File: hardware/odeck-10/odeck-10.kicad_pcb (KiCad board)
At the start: 6 copper layers, 110 x 75 mm, 4 parts

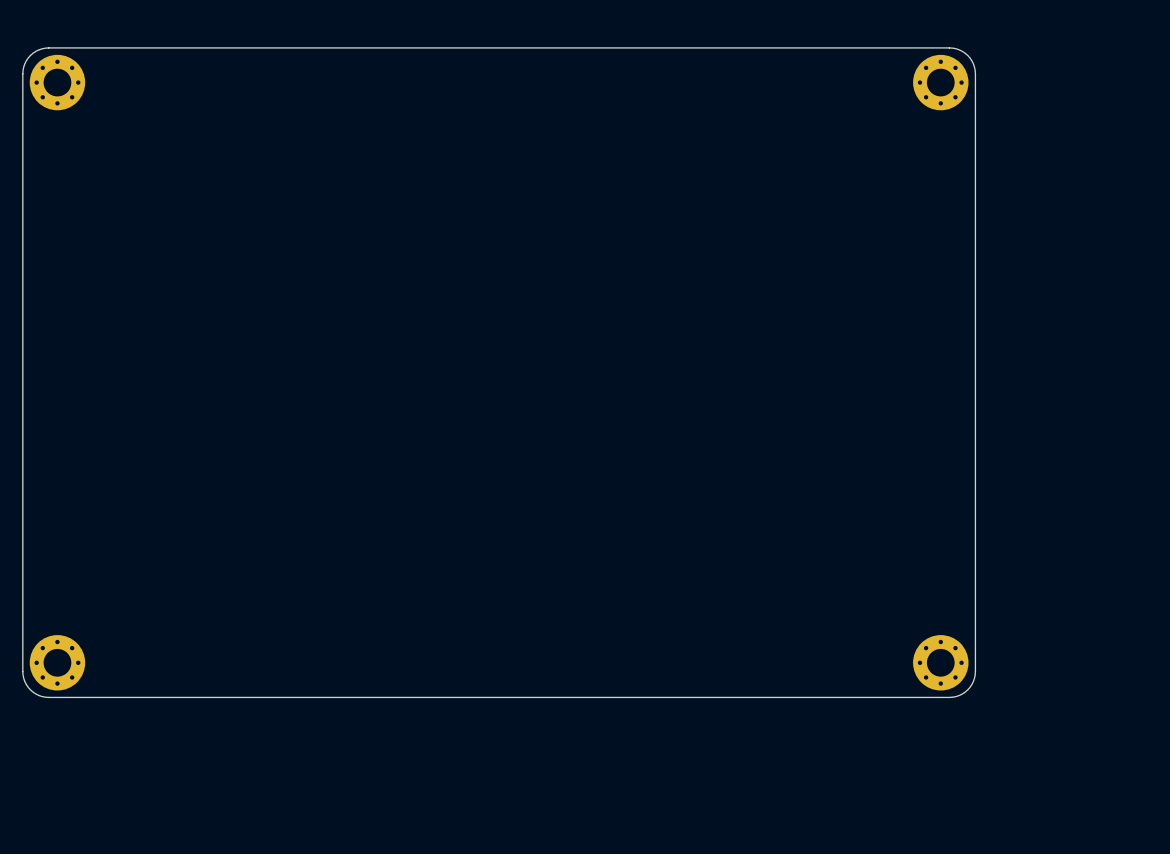
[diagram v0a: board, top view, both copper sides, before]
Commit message: Cost pass, PCB sync + rough placement, renders, README
- cost pass: extended parts 129 -> 114 (~$45/order less), nets unchanged
- tools/pcbsync.py: scripted update-PCB-from-schematic (keeps placed parts)
- tools/set_outline.py; board grown to 130x85 mm (provisional)
- hardware/odeck-10/placement.py: edge connectors + anchor-based packing,
  small passives spill to bottom; all 796 parts on the board (2 at anchor)
- docs/images: top/bottom/iso renders of the rough placement
- README.md: overview, architecture, repo layout, workflow, roadmap

Co-Authored-By: Claude Opus 5.5 <noreply@anthropic.com>
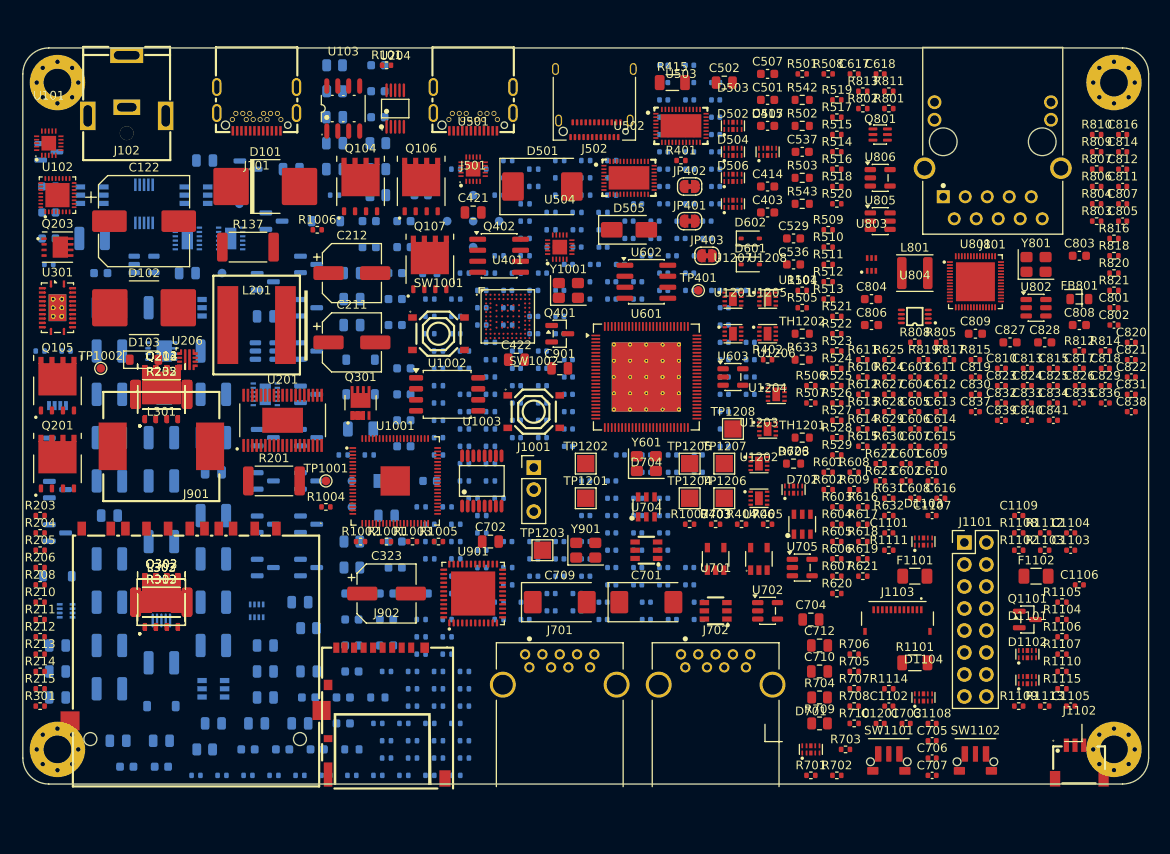
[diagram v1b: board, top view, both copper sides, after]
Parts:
- added C1001: 4.7u, Capacitor_SMD:C_0402_1005Metric, B.Cu at (156.0, 107.0)
- added C1002: 4.7u, Capacitor_SMD:C_0402_1005Metric, B.Cu at (157.0, 95.0)
- added C1003: 4.7u, Capacitor_SMD:C_0402_1005Metric, B.Cu at (157.0, 93.0)
- added C1004: 4.7u, Capacitor_SMD:C_0402_1005Metric, B.Cu at (157.0, 91.0)
- added C1005: 100n, Capacitor_SMD:C_0402_1005Metric, B.Cu at (157.0, 89.0)
- added C1006: 10u, Capacitor_SMD:C_0603_1608Metric, B.Cu at (144.0, 96.0)
- added C1007: 100n, Capacitor_SMD:C_0402_1005Metric, B.Cu at (157.0, 87.0)
- added C1008: 100n, Capacitor_SMD:C_0402_1005Metric, B.Cu at (157.0, 85.0)
- added C1009: 100n, Capacitor_SMD:C_0402_1005Metric, B.Cu at (158.0, 114.0)
- added C101: 2.2u/100V, Capacitor_SMD:C_1210_3225Metric, B.Cu at (108.0, 72.0)
- added C1010: 100n, Capacitor_SMD:C_0402_1005Metric, B.Cu at (158.0, 116.0)
- added C1011: 100n, Capacitor_SMD:C_0402_1005Metric, B.Cu at (159.0, 107.0)
- added C1012: 100n, Capacitor_SMD:C_0402_1005Metric, B.Cu at (159.0, 109.0)
- added C1013: 100n, Capacitor_SMD:C_0402_1005Metric, B.Cu at (159.0, 111.0)
- added C1014: 100n, Capacitor_SMD:C_0402_1005Metric, B.Cu at (159.0, 83.0)
- added C1015: 100n, Capacitor_SMD:C_0402_1005Metric, B.Cu at (160.0, 95.0)
- added C1016: 100n, Capacitor_SMD:C_0402_1005Metric, B.Cu at (160.0, 93.0)
- added C1017: 100n, Capacitor_SMD:C_0402_1005Metric, B.Cu at (160.0, 91.0)
- added C1018: 100n, Capacitor_SMD:C_0402_1005Metric, B.Cu at (160.0, 89.0)
- added C1019: 100n, Capacitor_SMD:C_0402_1005Metric, B.Cu at (160.0, 87.0)
- added C102: 100n/100V, Capacitor_SMD:C_0805_2012Metric, B.Cu at (121.0, 63.0)
- added C1020: 15p, Capacitor_SMD:C_0402_1005Metric, B.Cu at (160.0, 85.0)
- added C1021: 15p, Capacitor_SMD:C_0402_1005Metric, B.Cu at (161.0, 113.0)
- added C1022: 100n, Capacitor_SMD:C_0402_1005Metric, B.Cu at (161.0, 115.0)
- added C1023: 100n, Capacitor_SMD:C_0402_1005Metric, B.Cu at (159.0, 81.0)
- added C1024: 10n, Capacitor_SMD:C_0402_1005Metric, B.Cu at (162.0, 107.0)
- added C1025: 10n, Capacitor_SMD:C_0402_1005Metric, B.Cu at (162.0, 109.0)
- added C1026: 100n, Capacitor_SMD:C_0402_1005Metric, B.Cu at (162.0, 111.0)
- added C1027: 100n, Capacitor_SMD:C_0402_1005Metric, B.Cu at (162.0, 83.0)
- added C1028: 4.7u, Capacitor_SMD:C_0402_1005Metric, B.Cu at (162.0, 81.0)
- added C103: 100n/100V, Capacitor_SMD:C_0805_2012Metric, B.Cu at (119.0, 76.0)
- added C104: 1u, Capacitor_SMD:C_0402_1005Metric, B.Cu at (156.0, 78.0)
- added C105: 100n/50V, Capacitor_SMD:C_0603_1608Metric, B.Cu at (103.0, 66.0)
- added C106: 10u, Capacitor_SMD:C_0603_1608Metric, B.Cu at (103.0, 69.0)
- added C107: 10u, Capacitor_SMD:C_0603_1608Metric, B.Cu at (103.0, 72.0)
- added C108: 10u, Capacitor_SMD:C_0603_1608Metric, B.Cu at (109.0, 76.0)
- added C109: 220p, Capacitor_SMD:C_0603_1608Metric, B.Cu at (140.0, 70.0)
- added C110: 220p, Capacitor_SMD:C_0603_1608Metric, B.Cu at (140.0, 73.0)
- added C1101: 4.7u, Capacitor_SMD:C_0402_1005Metric, F.Cu at (200.0, 106.0)
- added C1102: 100n, Capacitor_SMD:C_0402_1005Metric, F.Cu at (200.0, 126.0)
- added C1103: 10n, Capacitor_SMD:C_0402_1005Metric, F.Cu at (221.0, 108.0)
- added C1104: 10n, Capacitor_SMD:C_0402_1005Metric, F.Cu at (221.0, 106.0)
- added C1105: 100n, Capacitor_SMD:C_0402_1005Metric, F.Cu at (221.0, 126.0)
- added C1106: 100n, Capacitor_SMD:C_0402_1005Metric, F.Cu at (222.0, 112.0)
- added C1107: 100n, Capacitor_SMD:C_0402_1005Metric, F.Cu at (205.0, 104.0)
- added C1108: 10n, Capacitor_SMD:C_0402_1005Metric, F.Cu at (205.0, 128.0)
- added C1109: 10n, Capacitor_SMD:C_0402_1005Metric, F.Cu at (215.0, 104.0)
- added C111: 100n, Capacitor_SMD:C_0402_1005Metric, B.Cu at (159.0, 78.0)
- added C112: 100n/100V, Capacitor_SMD:C_0805_2012Metric, B.Cu at (131.0, 64.0)
- added C113: 100n/50V, Capacitor_SMD:C_0603_1608Metric, B.Cu at (141.0, 58.0)
- added C114: 47n/100V, Capacitor_SMD:C_0603_1608Metric, B.Cu at (141.0, 55.0)
- added C115: 100n/100V, Capacitor_SMD:C_0805_2012Metric, B.Cu at (128.0, 81.0)
- added C116: 100n/100V, Capacitor_SMD:C_0805_2012Metric, B.Cu at (136.0, 64.0)
- added C117: 100n/50V, Capacitor_SMD:C_0603_1608Metric, B.Cu at (141.0, 52.0)
- added C118: 47n/100V, Capacitor_SMD:C_0603_1608Metric, B.Cu at (143.0, 76.0)
- added C119: 100n, Capacitor_SMD:C_0402_1005Metric, B.Cu at (160.0, 76.0)
- added C120: 100n, Capacitor_SMD:C_0402_1005Metric, B.Cu at (161.0, 73.0)
- added C1201: 100n, Capacitor_SMD:C_0402_1005Metric, F.Cu at (199.0, 128.0)
- added C1202: 100n, Capacitor_SMD:C_0402_1005Metric, B.Cu at (165.0, 102.0)
- added C1203: 100n, Capacitor_SMD:C_0402_1005Metric, B.Cu at (165.0, 100.0)
- added C1204: 100n, Capacitor_SMD:C_0402_1005Metric, B.Cu at (165.0, 104.0)
- added C1205: 100n, Capacitor_SMD:C_0402_1005Metric, B.Cu at (168.0, 102.0)
- added C1206: 100n, Capacitor_SMD:C_0402_1005Metric, B.Cu at (168.0, 100.0)
- added C1207: 100n, Capacitor_SMD:C_0402_1005Metric, B.Cu at (168.0, 104.0)
- added C1208: 100n, Capacitor_SMD:C_0402_1005Metric, B.Cu at (165.0, 98.0)
- added C121: 100n, Capacitor_SMD:C_0402_1005Metric, B.Cu at (162.0, 78.0)
- added C122: 47u/100V, Capacitor_SMD:CP_Elec_10x10, F.Cu at (114.0, 70.0)
- added C123: 1u/100V, Capacitor_SMD:C_0805_2012Metric, B.Cu at (136.0, 61.0)
- added C124: 100n/100V, Capacitor_SMD:C_0805_2012Metric, B.Cu at (136.0, 58.0)
- added C125: 100n, Capacitor_SMD:C_0402_1005Metric, B.Cu at (163.0, 75.0)
- added C201: 4.7u/100V, Capacitor_SMD:C_1210_3225Metric, B.Cu at (116.0, 95.0)
- added C202: 4.7u/100V, Capacitor_SMD:C_1210_3225Metric, B.Cu at (110.0, 90.0)
- added C203: 4.7u/100V, Capacitor_SMD:C_1210_3225Metric, B.Cu at (122.0, 90.0)
- added C204: 4.7u/100V, Capacitor_SMD:C_1210_3225Metric, B.Cu at (110.0, 85.0)
- added C205: 10u/50V, Capacitor_SMD:C_1210_3225Metric, B.Cu at (122.0, 85.0)
- added C206: 10u/50V, Capacitor_SMD:C_1210_3225Metric, B.Cu at (110.0, 95.0)
- added C207: 10u/50V, Capacitor_SMD:C_1210_3225Metric, B.Cu at (122.0, 95.0)
- added C208: 10u/50V, Capacitor_SMD:C_1210_3225Metric, B.Cu at (116.0, 80.0)
- added C209: 10u/50V, Capacitor_SMD:C_1210_3225Metric, B.Cu at (116.0, 100.0)
- added C210: 10u/50V, Capacitor_SMD:C_1210_3225Metric, B.Cu at (110.0, 80.0)
- added C211: 100u/35V, Capacitor_SMD:CP_Elec_6.3x7.7, F.Cu at (138.0, 84.0)
- added C212: 100u/35V, Capacitor_SMD:CP_Elec_6.3x7.7, F.Cu at (138.0, 76.0)
- added C213: 100n/50V, Capacitor_SMD:C_0603_1608Metric, B.Cu at (138.0, 113.0)
- added C214: 100n/100V, Capacitor_SMD:C_0805_2012Metric, B.Cu at (122.0, 99.0)
- added C215: 1u/100V, Capacitor_SMD:C_0805_2012Metric, B.Cu at (110.0, 104.0)
- added C216: 1u/50V, Capacitor_SMD:C_0603_1608Metric, B.Cu at (138.0, 116.0)
- added C217: 22u, Capacitor_SMD:C_0805_2012Metric, B.Cu at (138.0, 82.0)
- added C218: 22u, Capacitor_SMD:C_0805_2012Metric, B.Cu at (138.0, 79.0)
- added C219: 100n/50V, Capacitor_SMD:C_0603_1608Metric, B.Cu at (142.0, 113.0)
- added C220: 100n/50V, Capacitor_SMD:C_0603_1608Metric, B.Cu at (142.0, 116.0)
- added C221: 100p, Capacitor_SMD:C_0402_1005Metric, B.Cu at (163.0, 90.0)
- added C222: 22n, Capacitor_SMD:C_0402_1005Metric, B.Cu at (163.0, 88.0)
- added C223: 6.8n, Capacitor_SMD:C_0603_1608Metric, B.Cu at (143.0, 82.0)
- added C224: 82p, Capacitor_SMD:C_0402_1005Metric, B.Cu at (163.0, 92.0)
- added C225: 1n, Capacitor_SMD:C_0402_1005Metric, B.Cu at (163.0, 86.0)
- added C226: 4.7u, Capacitor_SMD:C_0603_1608Metric, B.Cu at (143.0, 79.0)
- added C227: 4.7n, Capacitor_SMD:C_0402_1005Metric, B.Cu at (163.0, 94.0)
- added C228: 100n/50V, Capacitor_SMD:C_0603_1608Metric, B.Cu at (143.0, 107.0)
- added C229: 100n/50V, Capacitor_SMD:C_0603_1608Metric, B.Cu at (143.0, 110.0)
- added C230: 22n/50V, Capacitor_SMD:C_0603_1608Metric, B.Cu at (144.0, 90.0)
- added C231: 100n, Capacitor_SMD:C_0402_1005Metric, B.Cu at (163.0, 96.0)
- added C232: 100n, Capacitor_SMD:C_0402_1005Metric, B.Cu at (164.0, 73.0)
- added C233: 10u/50V, Capacitor_SMD:C_1210_3225Metric, B.Cu at (110.0, 100.0)
- added C234: 100n/50V, Capacitor_SMD:C_0603_1608Metric, B.Cu at (144.0, 87.0)
- added C235: 100n/50V, Capacitor_SMD:C_0603_1608Metric, B.Cu at (144.0, 93.0)
- added C236: 100n/50V, Capacitor_SMD:C_0603_1608Metric, B.Cu at (144.0, 73.0)
- added C237: 100n/50V, Capacitor_SMD:C_0603_1608Metric, B.Cu at (144.0, 70.0)
- added C238: 1u/50V, Capacitor_SMD:C_0603_1608Metric, B.Cu at (138.0, 119.0)
- added C239: 3.3n, Capacitor_SMD:C_0603_1608Metric, B.Cu at (142.0, 119.0)
- added C240: 1n, Capacitor_SMD:C_0402_1005Metric, B.Cu at (164.0, 71.0)
- added C241: 10u, Capacitor_SMD:C_0805_2012Metric, B.Cu at (138.0, 76.0)
- added C242: 100n, Capacitor_SMD:C_0402_1005Metric, B.Cu at (164.0, 113.0)
- added C243: 2.2n, Capacitor_SMD:C_0603_1608Metric, B.Cu at (146.0, 67.0)
- added C244: 100n, Capacitor_SMD:C_0402_1005Metric, B.Cu at (164.0, 115.0)
- added C301: 4.7u/100V, Capacitor_SMD:C_1210_3225Metric, B.Cu at (110.0, 114.0)
- added C302: 4.7u/100V, Capacitor_SMD:C_1210_3225Metric, B.Cu at (122.0, 114.0)
- added C303: 4.7u/100V, Capacitor_SMD:C_1210_3225Metric, B.Cu at (110.0, 109.0)
- added C304: 4.7u/100V, Capacitor_SMD:C_1210_3225Metric, B.Cu at (122.0, 109.0)
- added C305: 100n/100V, Capacitor_SMD:C_0805_2012Metric, B.Cu at (104.0, 119.0)
- added C306: 100n/100V, Capacitor_SMD:C_0805_2012Metric, B.Cu at (128.0, 119.0)
- added C307: 100n, Capacitor_SMD:C_0402_1005Metric, B.Cu at (165.0, 111.0)
- added C308: 1n/100V, Capacitor_SMD:C_0603_1608Metric, B.Cu at (126.0, 131.0)
- added C309: 47u/10V, Capacitor_SMD:C_1210_3225Metric, B.Cu at (110.0, 119.0)
- added C310: 47u/10V, Capacitor_SMD:C_1210_3225Metric, B.Cu at (122.0, 119.0)
- added C311: 47u/10V, Capacitor_SMD:C_1210_3225Metric, B.Cu at (116.0, 107.0)
- added C312: 47u/10V, Capacitor_SMD:C_1210_3225Metric, B.Cu at (116.0, 121.0)
- added C313: 47u/10V, Capacitor_SMD:C_1210_3225Metric, B.Cu at (110.0, 124.0)
- added C314: 47u/10V, Capacitor_SMD:C_1210_3225Metric, B.Cu at (122.0, 104.0)
- added C315: 1u/100V, Capacitor_SMD:C_0805_2012Metric, B.Cu at (104.0, 122.0)
- added C316: 4.7u, Capacitor_SMD:C_0603_1608Metric, B.Cu at (133.0, 125.0)
- added C317: 100n, Capacitor_SMD:C_0402_1005Metric, B.Cu at (165.0, 109.0)
- added C318: 10n, Capacitor_SMD:C_0402_1005Metric, B.Cu at (165.0, 107.0)
- added C319: 100p, Capacitor_SMD:C_0402_1005Metric, B.Cu at (165.0, 79.0)
- added C320: 100n/50V, Capacitor_SMD:C_0603_1608Metric, B.Cu at (130.0, 131.0)
- added C321: 100n/50V, Capacitor_SMD:C_0603_1608Metric, B.Cu at (134.0, 131.0)
- added C322: 100n, Capacitor_SMD:C_0402_1005Metric, B.Cu at (165.0, 77.0)
- added C323: 330u/6.3V, Capacitor_SMD:CP_Elec_6.3x5.9, F.Cu at (142.0, 113.0)
- added C324: 22u, Capacitor_SMD:C_0805_2012Metric, B.Cu at (128.0, 122.0)
- added C325: 22u, Capacitor_SMD:C_0805_2012Metric, B.Cu at (104.0, 125.0)
- added C326: 10u, Capacitor_SMD:C_0805_2012Metric, B.Cu at (128.0, 125.0)
- added C327: 10u, Capacitor_SMD:C_0805_2012Metric, B.Cu at (122.0, 128.0)
- added C328: 100n, Capacitor_SMD:C_0402_1005Metric, B.Cu at (166.0, 75.0)
- added C329: 22n, Capacitor_SMD:C_0402_1005Metric, B.Cu at (167.0, 114.0)
- added C330: 100n, Capacitor_SMD:C_0402_1005Metric, B.Cu at (167.0, 116.0)
- added C331: 22u, Capacitor_SMD:C_0805_2012Metric, B.Cu at (127.0, 128.0)
- added C332: 22u, Capacitor_SMD:C_0805_2012Metric, B.Cu at (116.0, 130.0)
- added C333: 22u, Capacitor_SMD:C_0805_2012Metric, B.Cu at (132.0, 114.0)
- added C334: 10u, Capacitor_SMD:C_0805_2012Metric, B.Cu at (111.0, 130.0)
- added C335: 10u, Capacitor_SMD:C_0805_2012Metric, B.Cu at (132.0, 128.0)
- added C336: 100n, Capacitor_SMD:C_0402_1005Metric, B.Cu at (167.0, 73.0)
- added C337: 100n, Capacitor_SMD:C_0402_1005Metric, B.Cu at (167.0, 71.0)
- added C338: 22u, Capacitor_SMD:C_0603_1608Metric, B.Cu at (116.0, 133.0)
- added C339: 22u, Capacitor_SMD:C_0603_1608Metric, B.Cu at (112.0, 133.0)
- added C340: 22u, Capacitor_SMD:C_0603_1608Metric, B.Cu at (137.0, 125.0)
- added C341: 22u, Capacitor_SMD:C_0603_1608Metric, B.Cu at (137.0, 128.0)
- added C401: 1u, Capacitor_SMD:C_0402_1005Metric, B.Cu at (168.0, 77.0)
- added C402: 100n, Capacitor_SMD:C_0402_1005Metric, B.Cu at (168.0, 79.0)
- added C403: 4.7u, Capacitor_SMD:C_0603_1608Metric, F.Cu at (186.0, 69.0)
- added C404: 100n, Capacitor_SMD:C_0402_1005Metric, B.Cu at (169.0, 75.0)
- added C405: 1u, Capacitor_SMD:C_0402_1005Metric, B.Cu at (170.0, 70.0)
- added C406: 100n, Capacitor_SMD:C_0402_1005Metric, B.Cu at (170.0, 72.0)
- added C407: 100n, Capacitor_SMD:C_0402_1005Metric, B.Cu at (171.0, 68.0)
- added C408: 1u, Capacitor_SMD:C_0402_1005Metric, B.Cu at (171.0, 66.0)
- added C409: 100n, Capacitor_SMD:C_0402_1005Metric, B.Cu at (171.0, 64.0)
- added C410: 100n, Capacitor_SMD:C_0402_1005Metric, B.Cu at (171.0, 77.0)
- added C411: 100n, Capacitor_SMD:C_0402_1005Metric, B.Cu at (171.0, 79.0)
- added C412: 1u, Capacitor_SMD:C_0402_1005Metric, B.Cu at (172.0, 74.0)
- added C413: 1u, Capacitor_SMD:C_0402_1005Metric, B.Cu at (173.0, 70.0)
- added C414: 100n/50V, Capacitor_SMD:C_0603_1608Metric, F.Cu at (186.0, 66.0)
- added C415: 100n/50V, Capacitor_SMD:C_0603_1608Metric, F.Cu at (186.0, 59.0)
- added C416: 390p, Capacitor_SMD:C_0402_1005Metric, B.Cu at (173.0, 72.0)
- added C417: 390p, Capacitor_SMD:C_0402_1005Metric, B.Cu at (174.0, 68.0)
- added C418: 390p, Capacitor_SMD:C_0402_1005Metric, B.Cu at (174.0, 66.0)
- added C419: 390p, Capacitor_SMD:C_0402_1005Metric, B.Cu at (174.0, 64.0)
- added C420: 100n, Capacitor_SMD:C_0402_1005Metric, B.Cu at (174.0, 76.0)
- added C421: 10u, Capacitor_SMD:C_0805_2012Metric, F.Cu at (152.0, 69.0)
- added C422: 10u, Capacitor_SMD:C_0805_2012Metric, F.Cu at (157.0, 86.0)
- added C501: 100n/50V, Capacitor_SMD:C_0603_1608Metric, F.Cu at (186.0, 56.0)
- added C502: 100n/100V, Capacitor_SMD:C_0805_2012Metric, F.Cu at (181.0, 54.0)
- added C503: 1u, Capacitor_SMD:C_0402_1005Metric, B.Cu at (174.0, 62.0)
- added C504: 100n, Capacitor_SMD:C_0402_1005Metric, B.Cu at (174.0, 60.0)
- added C505: 100n, Capacitor_SMD:C_0402_1005Metric, B.Cu at (174.0, 58.0)
- added C506: 100n, Capacitor_SMD:C_0402_1005Metric, B.Cu at (174.0, 56.0)
- added C507: 10u, Capacitor_SMD:C_0603_1608Metric, F.Cu at (186.0, 53.0)
- added C508: 100n, Capacitor_SMD:C_0402_1005Metric, B.Cu at (174.0, 54.0)
- added C509: 220n, Capacitor_SMD:C_0402_1005Metric, B.Cu at (174.0, 52.0)
- added C510: 220n, Capacitor_SMD:C_0402_1005Metric, B.Cu at (175.0, 74.0)
- added C511: 220n, Capacitor_SMD:C_0402_1005Metric, B.Cu at (176.0, 70.0)
- added C512: 220n, Capacitor_SMD:C_0402_1005Metric, B.Cu at (176.0, 72.0)
- added C513: 220n, Capacitor_SMD:C_0402_1005Metric, B.Cu at (174.0, 78.0)
- added C514: 220n, Capacitor_SMD:C_0402_1005Metric, B.Cu at (177.0, 62.0)
- added C515: 220n, Capacitor_SMD:C_0402_1005Metric, B.Cu at (177.0, 60.0)
- added C516: 220n, Capacitor_SMD:C_0402_1005Metric, B.Cu at (177.0, 64.0)
- added C517: 220n, Capacitor_SMD:C_0402_1005Metric, B.Cu at (177.0, 58.0)
- added C518: 220n, Capacitor_SMD:C_0402_1005Metric, B.Cu at (177.0, 66.0)
- added C519: 220n, Capacitor_SMD:C_0402_1005Metric, B.Cu at (177.0, 56.0)
- added C520: 220n, Capacitor_SMD:C_0402_1005Metric, B.Cu at (177.0, 68.0)
- added C521: 220n, Capacitor_SMD:C_0402_1005Metric, B.Cu at (177.0, 54.0)
- added C522: 220n, Capacitor_SMD:C_0402_1005Metric, B.Cu at (177.0, 52.0)
- added C523: 100n, Capacitor_SMD:C_0402_1005Metric, B.Cu at (177.0, 76.0)
- added C524: 100n, Capacitor_SMD:C_0402_1005Metric, B.Cu at (177.0, 78.0)
- added C525: 100n, Capacitor_SMD:C_0402_1005Metric, B.Cu at (178.0, 74.0)
- added C526: 100n, Capacitor_SMD:C_0402_1005Metric, B.Cu at (179.0, 70.0)
- added C527: 100n, Capacitor_SMD:C_0402_1005Metric, B.Cu at (179.0, 72.0)
- added C528: 100n, Capacitor_SMD:C_0402_1005Metric, B.Cu at (180.0, 62.0)
- added C529: 10u, Capacitor_SMD:C_0603_1608Metric, F.Cu at (189.0, 72.0)
- added C530: 220n, Capacitor_SMD:C_0402_1005Metric, B.Cu at (180.0, 60.0)
- added C531: 220n, Capacitor_SMD:C_0402_1005Metric, B.Cu at (180.0, 64.0)
- added C532: 220n, Capacitor_SMD:C_0402_1005Metric, B.Cu at (180.0, 58.0)
- added C533: 220n, Capacitor_SMD:C_0402_1005Metric, B.Cu at (180.0, 66.0)
- added C534: 220n, Capacitor_SMD:C_0402_1005Metric, B.Cu at (180.0, 56.0)
- added C535: 220n, Capacitor_SMD:C_0402_1005Metric, B.Cu at (180.0, 68.0)
- added C536: 100n/50V, Capacitor_SMD:C_0603_1608Metric, F.Cu at (189.0, 75.0)
- added C537: 100n/50V, Capacitor_SMD:C_0603_1608Metric, F.Cu at (190.0, 62.0)
- added C538: 1u, Capacitor_SMD:C_0402_1005Metric, B.Cu at (180.0, 54.0)
- added C601: 220n, Capacitor_SMD:C_0402_1005Metric, F.Cu at (202.0, 98.0)
- added C602: 220n, Capacitor_SMD:C_0402_1005Metric, F.Cu at (202.0, 100.0)
- added C603: 220n, Capacitor_SMD:C_0402_1005Metric, F.Cu at (203.0, 88.0)
- added C604: 220n, Capacitor_SMD:C_0402_1005Metric, F.Cu at (203.0, 90.0)
- added C605: 220n, Capacitor_SMD:C_0402_1005Metric, F.Cu at (203.0, 92.0)
- added C606: 220n, Capacitor_SMD:C_0402_1005Metric, F.Cu at (203.0, 94.0)
- added C607: 220n, Capacitor_SMD:C_0402_1005Metric, F.Cu at (203.0, 96.0)
- added C608: 220n, Capacitor_SMD:C_0402_1005Metric, F.Cu at (203.0, 102.0)
- added C609: 220n, Capacitor_SMD:C_0402_1005Metric, F.Cu at (205.0, 98.0)
- added C610: 220n, Capacitor_SMD:C_0402_1005Metric, F.Cu at (205.0, 100.0)
- added C611: 220n, Capacitor_SMD:C_0402_1005Metric, F.Cu at (206.0, 88.0)
- added C612: 220n, Capacitor_SMD:C_0402_1005Metric, F.Cu at (206.0, 90.0)
- added C613: 100n, Capacitor_SMD:C_0402_1005Metric, F.Cu at (206.0, 92.0)
- added C614: 100n, Capacitor_SMD:C_0402_1005Metric, F.Cu at (206.0, 94.0)
- added C615: 100n, Capacitor_SMD:C_0402_1005Metric, F.Cu at (206.0, 96.0)
- added C616: 100n, Capacitor_SMD:C_0402_1005Metric, F.Cu at (206.0, 102.0)
- added C617: 100n, Capacitor_SMD:C_0402_1005Metric, F.Cu at (196.0, 53.0)
- added C618: 100n, Capacitor_SMD:C_0402_1005Metric, F.Cu at (199.0, 53.0)
- added C619: 100n, Capacitor_SMD:C_0402_1005Metric, B.Cu at (172.0, 97.0)
- added C620: 100n, Capacitor_SMD:C_0402_1005Metric, B.Cu at (181.0, 88.0)
- added C621: 4.7u, Capacitor_SMD:C_0402_1005Metric, B.Cu at (181.0, 86.0)
- added C622: 4.7u, Capacitor_SMD:C_0402_1005Metric, B.Cu at (181.0, 90.0)
- added C623: 1n, Capacitor_SMD:C_0402_1005Metric, B.Cu at (169.0, 97.0)
- added C624: 100n, Capacitor_SMD:C_0402_1005Metric, B.Cu at (175.0, 97.0)
- added C625: 100n, Capacitor_SMD:C_0402_1005Metric, B.Cu at (181.0, 84.0)
- added C626: 100n, Capacitor_SMD:C_0402_1005Metric, B.Cu at (181.0, 92.0)
- added C627: 100n, Capacitor_SMD:C_0402_1005Metric, B.Cu at (181.0, 82.0)
- added C628: 100n, Capacitor_SMD:C_0402_1005Metric, B.Cu at (178.0, 97.0)
- added C629: 100n, Capacitor_SMD:C_0402_1005Metric, B.Cu at (181.0, 94.0)
- added C630: 100n, Capacitor_SMD:C_0402_1005Metric, B.Cu at (181.0, 80.0)
- added C631: 100n, Capacitor_SMD:C_0402_1005Metric, B.Cu at (181.0, 96.0)
- added C632: 100n, Capacitor_SMD:C_0402_1005Metric, B.Cu at (180.0, 78.0)
- added C633: 4.7u, Capacitor_SMD:C_0402_1005Metric, B.Cu at (181.0, 98.0)
- added C634: 4.7u, Capacitor_SMD:C_0402_1005Metric, B.Cu at (172.0, 99.0)
- added C635: 4.7u, Capacitor_SMD:C_0402_1005Metric, B.Cu at (175.0, 99.0)
- added C636: 1n, Capacitor_SMD:C_0402_1005Metric, B.Cu at (178.0, 99.0)
- added C637: 20p, Capacitor_SMD:C_0402_1005Metric, B.Cu at (183.0, 78.0)
- added C638: 20p, Capacitor_SMD:C_0402_1005Metric, B.Cu at (184.0, 88.0)
- added C639: 1n, Capacitor_SMD:C_0402_1005Metric, B.Cu at (184.0, 86.0)
- added C640: 100n, Capacitor_SMD:C_0402_1005Metric, B.Cu at (184.0, 90.0)
- added C641: 100n, Capacitor_SMD:C_0402_1005Metric, B.Cu at (184.0, 84.0)
- added C701: 150u/10V, Capacitor_Tantalum_SMD:CP_EIA-7343-31_Kemet-D, F.Cu at (172.0, 114.0)
- added C702: 10u, Capacitor_SMD:C_0805_2012Metric, F.Cu at (154.0, 107.0)
- added C703: 100n, Capacitor_SMD:C_0402_1005Metric, F.Cu at (202.0, 128.0)
- added C704: 10u, Capacitor_SMD:C_0805_2012Metric, F.Cu at (191.0, 116.0)
- added C705: 100n, Capacitor_SMD:C_0402_1005Metric, F.Cu at (205.0, 130.0)
- added C706: 100n, Capacitor_SMD:C_0402_1005Metric, F.Cu at (205.0, 132.0)
- added C707: 100n, Capacitor_SMD:C_0402_1005Metric, F.Cu at (205.0, 134.0)
- added C708: 100n, Capacitor_SMD:C_0402_1005Metric, B.Cu at (172.0, 116.0)
- added C709: 150u/10V, Capacitor_Tantalum_SMD:CP_EIA-7343-31_Kemet-D, F.Cu at (162.0, 114.0)
- added C710: 10u, Capacitor_SMD:C_0805_2012Metric, F.Cu at (192.0, 122.0)
- added C711: 100n, Capacitor_SMD:C_0402_1005Metric, B.Cu at (175.0, 116.0)
- added C712: 10u, Capacitor_SMD:C_0805_2012Metric, F.Cu at (192.0, 119.0)
- added C713: 100n, Capacitor_SMD:C_0402_1005Metric, B.Cu at (178.0, 116.0)
- added C714: 100n, Capacitor_SMD:C_0402_1005Metric, B.Cu at (172.0, 114.0)
- added C715: 100n, Capacitor_SMD:C_0402_1005Metric, B.Cu at (175.0, 114.0)
- added C716: 100n, Capacitor_SMD:C_0402_1005Metric, B.Cu at (178.0, 114.0)
- added C801: 1u, Capacitor_SMD:C_0402_1005Metric, F.Cu at (226.0, 80.0)
- added C802: 1n, Capacitor_SMD:C_0402_1005Metric, F.Cu at (226.0, 82.0)
- added C803: 10u, Capacitor_SMD:C_0603_1608Metric, F.Cu at (222.0, 74.0)
- added C804: 22u, Capacitor_SMD:C_0603_1608Metric, F.Cu at (198.0, 79.0)
- added C805: 100n, Capacitor_SMD:C_0402_1005Metric, F.Cu at (227.0, 70.0)
- added C806: 10u, Capacitor_SMD:C_0603_1608Metric, F.Cu at (198.0, 82.0)
- added C807: 100n, Capacitor_SMD:C_0402_1005Metric, F.Cu at (227.0, 68.0)
- added C808: 22u, Capacitor_SMD:C_0603_1608Metric, F.Cu at (222.0, 82.0)
- added C809: 22u, Capacitor_SMD:C_0603_1608Metric, F.Cu at (210.0, 83.0)
- added C810: 100n, Capacitor_SMD:C_0402_1005Metric, F.Cu at (213.0, 87.0)
- added C811: 2.2u, Capacitor_SMD:C_0402_1005Metric, F.Cu at (227.0, 66.0)
- added C812: 100n, Capacitor_SMD:C_0402_1005Metric, F.Cu at (227.0, 64.0)
- added C813: 100n, Capacitor_SMD:C_0402_1005Metric, F.Cu at (216.0, 87.0)
- added C814: 100n, Capacitor_SMD:C_0402_1005Metric, F.Cu at (227.0, 62.0)
- added C815: 2.2u, Capacitor_SMD:C_0402_1005Metric, F.Cu at (219.0, 87.0)
- added C816: 2.2u, Capacitor_SMD:C_0402_1005Metric, F.Cu at (227.0, 60.0)
- added C817: 100n, Capacitor_SMD:C_0402_1005Metric, F.Cu at (222.0, 87.0)
- added C818: 100n, Capacitor_SMD:C_0402_1005Metric, F.Cu at (225.0, 87.0)
- added C819: 100n, Capacitor_SMD:C_0402_1005Metric, F.Cu at (210.0, 88.0)
- added C820: 2.2u, Capacitor_SMD:C_0402_1005Metric, F.Cu at (228.0, 84.0)
- added C821: 2.2u, Capacitor_SMD:C_0402_1005Metric, F.Cu at (228.0, 86.0)
- added C822: 2.2u, Capacitor_SMD:C_0402_1005Metric, F.Cu at (228.0, 88.0)
- added C823: 100n, Capacitor_SMD:C_0402_1005Metric, F.Cu at (213.0, 89.0)
- added C824: 100n, Capacitor_SMD:C_0402_1005Metric, F.Cu at (216.0, 89.0)
- added C825: 100n, Capacitor_SMD:C_0402_1005Metric, F.Cu at (219.0, 89.0)
- added C826: 2.2u, Capacitor_SMD:C_0402_1005Metric, F.Cu at (222.0, 89.0)
- added C827: 10u, Capacitor_SMD:C_0603_1608Metric, F.Cu at (214.0, 84.0)
- added C828: 10u, Capacitor_SMD:C_0603_1608Metric, F.Cu at (218.0, 84.0)
- added C829: 100n, Capacitor_SMD:C_0402_1005Metric, F.Cu at (225.0, 89.0)
- added C830: 2.2u, Capacitor_SMD:C_0402_1005Metric, F.Cu at (210.0, 90.0)
- added C831: 100n, Capacitor_SMD:C_0402_1005Metric, F.Cu at (228.0, 90.0)
- added C832: 1u, Capacitor_SMD:C_0402_1005Metric, F.Cu at (213.0, 91.0)
- added C833: 20p, Capacitor_SMD:C_0402_1005Metric, F.Cu at (216.0, 91.0)
- added C834: 20p, Capacitor_SMD:C_0402_1005Metric, F.Cu at (219.0, 91.0)
- added C835: 100n, Capacitor_SMD:C_0402_1005Metric, F.Cu at (222.0, 91.0)
- added C836: 100n, Capacitor_SMD:C_0402_1005Metric, F.Cu at (225.0, 91.0)
- added C837: 390p, Capacitor_SMD:C_0402_1005Metric, F.Cu at (210.0, 92.0)
- added C838: 100n, Capacitor_SMD:C_0402_1005Metric, F.Cu at (228.0, 92.0)
- added C839: 100n, Capacitor_SMD:C_0402_1005Metric, F.Cu at (213.0, 93.0)
- added C840: 100n, Capacitor_SMD:C_0402_1005Metric, F.Cu at (216.0, 93.0)
- added C841: 100n, Capacitor_SMD:C_0402_1005Metric, F.Cu at (219.0, 93.0)
- added C901: 10u, Capacitor_SMD:C_0805_2012Metric, F.Cu at (162.0, 87.0)
- added C902: 100n, Capacitor_SMD:C_0402_1005Metric, B.Cu at (168.0, 112.0)
- added C903: 10u, Capacitor_SMD:C_0603_1608Metric, B.Cu at (138.0, 122.0)
- added C904: 1u, Capacitor_SMD:C_0402_1005Metric, B.Cu at (168.0, 110.0)
- added C905: 100n, Capacitor_SMD:C_0402_1005Metric, B.Cu at (168.0, 108.0)
- added C906: 100n, Capacitor_SMD:C_0402_1005Metric, B.Cu at (168.0, 106.0)
- added C907: 100n, Capacitor_SMD:C_0402_1005Metric, B.Cu at (171.0, 112.0)
- added C908: 100n, Capacitor_SMD:C_0402_1005Metric, B.Cu at (171.0, 110.0)
- added C909: 2.2u, Capacitor_SMD:C_0402_1005Metric, B.Cu at (171.0, 108.0)
- added C910: 1u, Capacitor_SMD:C_0402_1005Metric, B.Cu at (171.0, 106.0)
- added C911: 1u, Capacitor_SMD:C_0402_1005Metric, B.Cu at (171.0, 104.0)
- added C912: 1u, Capacitor_SMD:C_0402_1005Metric, B.Cu at (171.0, 102.0)
- added C913: 4.7u, Capacitor_SMD:C_0402_1005Metric, B.Cu at (174.0, 112.0)
- added C914: 100n, Capacitor_SMD:C_0402_1005Metric, B.Cu at (174.0, 110.0)
- added C915: 4.7u, Capacitor_SMD:C_0402_1005Metric, B.Cu at (174.0, 108.0)
- added C916: 100n, Capacitor_SMD:C_0402_1005Metric, B.Cu at (174.0, 106.0)
- added C917: 100n, Capacitor_SMD:C_0402_1005Metric, B.Cu at (174.0, 104.0)
- added C918: 100n, Capacitor_SMD:C_0402_1005Metric, B.Cu at (174.0, 102.0)
- added C919: 20p, Capacitor_SMD:C_0402_1005Metric, B.Cu at (177.0, 112.0)
- added C920: 20p, Capacitor_SMD:C_0402_1005Metric, B.Cu at (177.0, 110.0)
- added D1001: PWR green, LED_SMD:LED_0805_2012Metric, B.Cu at (142.0, 104.0)
- added D1002: STATUS red, LED_SMD:LED_0603_1608Metric, B.Cu at (147.0, 100.0)
- added D101: 5.0SMDJ51A, odeck:SMC_L6.9-W5.9-LS7.9-RD, F.Cu at (128.0, 66.0)
- added D102: 5.0SMDJ48CA, odeck:SMC_L6.9-W5.9-LS7.9-BI, F.Cu at (114.0, 80.0)
- added D103: 1N4148W, Diode_SMD:D_SOD-123, F.Cu at (114.0, 86.0)
- added D1101: TPD4E02B04, odeck:USON-10_L2.5-W1.0-P0.50-BL, F.Cu at (216.0, 120.0)
- added D1102: TPD4E02B04, odeck:USON-10_L2.5-W1.0-P0.50-BL, F.Cu at (216.0, 123.0)
- added D1103: TPD4E02B04, odeck:USON-10_L2.5-W1.0-P0.50-BL, F.Cu at (204.0, 107.0)
- added D1104: TPD4E02B04, odeck:USON-10_L2.5-W1.0-P0.50-BL, F.Cu at (204.0, 125.0)
- added D201: 1N4148W, Diode_SMD:D_SOD-123, B.Cu at (135.0, 70.0)
- added D202: BZT52C5V1, Diode_SMD:D_SOD-123, B.Cu at (104.0, 111.0)
- added D203: BAT54A, Package_TO_SOT_SMD:SOT-23, B.Cu at (128.0, 95.0)
- added D204: BAT46W, Diode_SMD:D_SOD-123, B.Cu at (139.0, 90.0)
- added D205: BAV70, Package_TO_SOT_SMD:SOT-23, B.Cu at (104.0, 96.0)
- added D206: 1N4148W, Diode_SMD:D_SOD-123, B.Cu at (139.0, 86.0)
- added D301: BAT46W, Diode_SMD:D_SOD-123, B.Cu at (116.0, 126.0)
- added D501: SMCJ28A, Diode_SMD:D_SMC, F.Cu at (160.0, 66.0)
- added D502: TPD4E02B04, odeck:USON-10_L2.5-W1.0-P0.50-BL, F.Cu at (182.0, 62.0)
- added D503: TPD4E02B04, odeck:USON-10_L2.5-W1.0-P0.50-BL, F.Cu at (182.0, 59.0)
- added D504: TPD4E02B04, odeck:USON-10_L2.5-W1.0-P0.50-BL, F.Cu at (182.0, 65.0)
- added D505: SMAJ6.0A, Diode_SMD:D_SMA, F.Cu at (170.0, 71.0)
- added D506: TPD4E02B04, odeck:USON-10_L2.5-W1.0-P0.50-BL, F.Cu at (182.0, 68.0)
- added D507: TPD4E02B04, odeck:USON-10_L2.5-W1.0-P0.50-BL, F.Cu at (186.0, 62.0)
- added D601: BAT54WS, Diode_SMD:D_SOD-323, F.Cu at (184.0, 75.0)
- added D602: BAT54WS, Diode_SMD:D_SOD-323, F.Cu at (184.0, 72.0)
- added D701: TPD4E02B04, odeck:USON-10_L2.5-W1.0-P0.50-BL, F.Cu at (191.0, 131.0)
- added D702: USBLC6-2SC6, odeck:SOT-23-6_L2.9-W1.6-P0.95-LS2.8-BL, F.Cu at (190.0, 105.0)
- added D703: TPD4E02B04, odeck:USON-10_L2.5-W1.0-P0.50-BL, F.Cu at (189.0, 101.0)
- added D704: USBLC6-2SC6, odeck:SOT-23-6_L2.9-W1.6-P0.95-LS2.8-BL, F.Cu at (172.0, 103.0)
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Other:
- board size 110 x 75 mm -> 130 x 85 mm

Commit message: Placement: floorplan, per-region placement scripts, DRC-clean placed board
- docs/floorplan.md: 5 regions; board 130x89 mm (SD socket depth), microSD on
  top at the front-right (overhangs edge 2 mm under the LCD panel)
- layout/{power,usbc,hubrails,front,right}.py + zz_integration.py; per-block
  placement rationale and routing intent in docs/layout-notes/
- tools/apply_layout.py (region/ownership/overlap checks), set_outline.py,
  pcbsync --refresh, apply_routing.py (coupled pairs, via pairs, zones),
  autoroute.py (Freerouting 2.4, headless, analytics off)
- schematic: R908 22R microSD CLK series termination
- footprints: PMG1 closed courtyard, barrel peg NPTH
- DRC rules (.kicad_dru): edge parts, HS pair spacing, HV clearance;
  HS netclass pad clearance 0.15
- DRC: 0 violations (499 unrouted, as expected); renders updated

Co-Authored-By: Claude Opus 5.5 <noreply@anthropic.com>
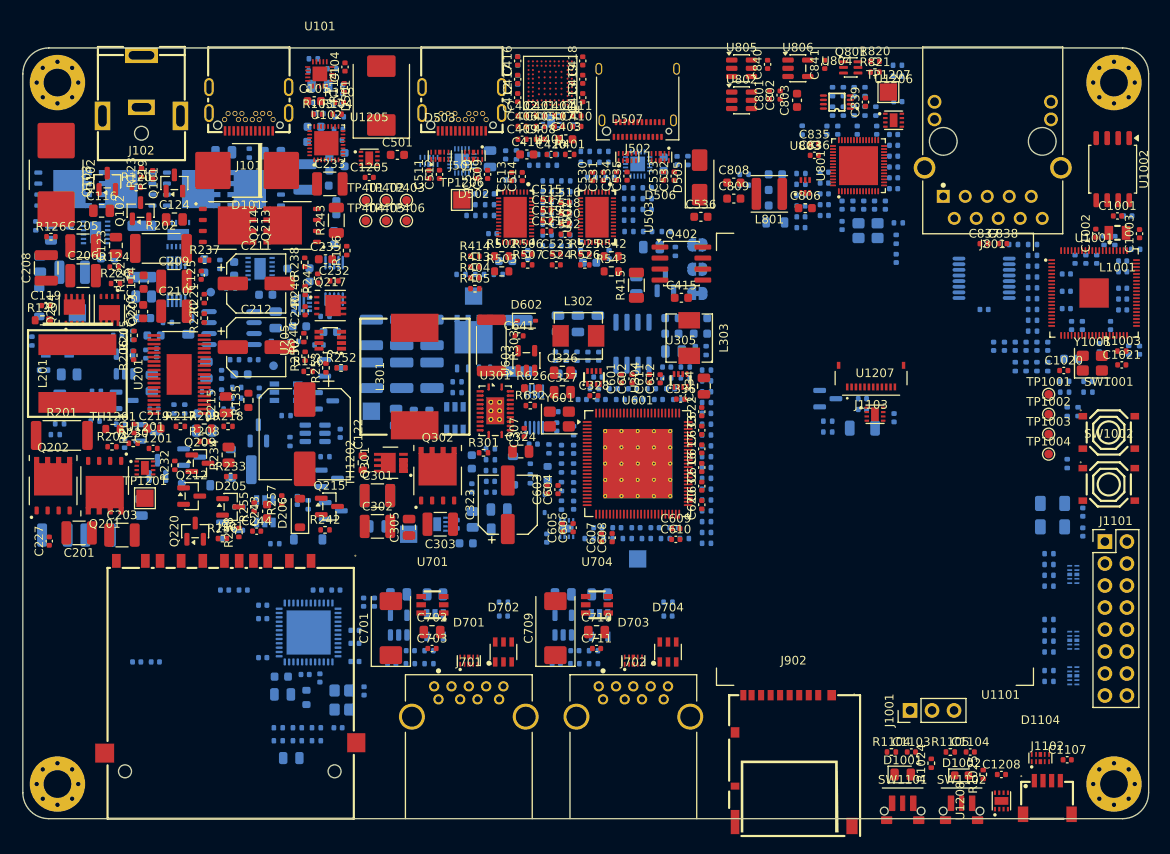
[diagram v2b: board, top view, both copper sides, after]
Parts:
- added R908: 22, Resistor_SMD:R_0402_1005Metric, B.Cu at (129.1, 107.2)
- C1001, C1002, C1003, C1020, C1021, C104, C105, C114, C116, C119, C1205, C1208, C123, C124, C125, C201, C203, C205, C206, C208, C209, C210, C215, C219, C220, C227, C232, C233, C235, C240, C243, C244, C301, C302, C303, C305, C307, C324, C326, C327, C328, C334, C336, C401, C402, C404, C405, C406, C407, C408, C409, C410, C411, C412, C413, C416, C417, C418, C419, C420, C509, C510, C511, C512, C513, C514, C515, C516, C517, C518, C519, C520, C521, C522, C523, C524, C530, C531, C532, C533, C534, C535, C620, C622, C632, C633, C641, C711, D1001, D1002, D205, D206, L1001, Q101, Q102, Q103, Q204, Q209, Q212, Q215, Q217, Q220, R1024, R1025, R103, R104, R110, R114, R116, R119, R120, R122, R123, R124, R126, R130, R135, R136, R209, R217, R218, R220, R221, R226, R230, R232, R233, R234, R237, R238, R242, R243, R244, R246, R247, R250, R252, R253, R255, R256, R257, R258, R413, R414, TP1003, TP1004, TP402, TP403, TP404, TP405, TP406, U205, U304, U305: moved to F.Cu
- C1101, C1102, C1105, C1106, C1108, C1109, C421, C422, C502, C507, C529, C537, C613, C614, C615, C618, C704, C705, C706, C707, C712, C804, C805, C807, C810, C811, C812, C813, C814, C815, C816, C817, C818, C819, C820, C821, C822, C823, C824, C825, C826, C827, C828, C829, C830, C831, C832, C833, C834, C901, D103, D1101, D1102, D1103, D504, D601, F1101, F1102, FB801, JP401, JP402, JP403, Q104, Q105, Q106, Q107, Q1101, Q303, Q401, R1001, R1002, R1004, R1005, R1006, R1007, R101, R1101, R1102, R1103, R1106, R1107, R1108, R1109, R1110, R1111, R1112, R1113, R1114, R1115, R137, R210, R211, R212, R213, R214, R215, R235, R312, R402, R403, R501, R504, R505, R508, R509, R510, R511, R512, R513, R514, R515, R516, R517, R518, R519, R520, R521, R522, R523, R524, R527, R528, R529, R601, R602, R603, R604, R605, R606, R607, R608, R609, R610, R611, R612, R613, R614, R615, R616, R617, R618, R619, R620, R621, R622, R623, R624, R625, R627, R628, R629, R630, R631, R633, R701, R702, R703, R704, R705, R706, R707, R708, R709, R710, R801, R802, R803, R804, R805, R806, R807, R808, R809, R810, R811, R812, R813, R814, R815, R816, R817, R818, R819, TP1202, TP1203, TP1204, TP1205, TP1208, U1003, U103, U1202, U1203, U1204, U204, U206, U501, U504, U602, U702, U703, U705, U706, U901, Y801, Y901: moved to B.Cu
- moved TP1002 109.6 mm to (218.4, 92.3)
- moved R1001 92.9 mm to (228.5, 73.2)
- moved R1002 91.4 mm to (227.7, 84.9), turned to 90 degrees
- moved R1006 90.7 mm to (220.6, 98.0), turned to 90 degrees
- moved C1201 89.8 mm to (115.0, 96.2)
- moved R1008 89.6 mm to (226.1, 72.2), turned to 90 degrees
- moved L1001 89.1 mm to (226.4, 71.3), turned to 180 degrees
- moved R1004 87.5 mm to (221.8, 92.0), turned to 90 degrees
- moved R1003 84.8 mm to (226.9, 85.0)
- moved C339 84.1 mm to (178.2, 81.2)
- moved TP1001 84.0 mm to (218.4, 90.0)
- moved U1001 83.6 mm to (223.7, 78.3)
- moved R1010 82.9 mm to (216.6, 74.0)
- moved U1002 81.1 mm to (225.8, 64.0), turned to -90 degrees
- moved C1022 80.7 mm to (227.6, 69.4)
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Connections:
- J902 pad 5: /Card reader/CR_USD_CLK -> /Card reader/CR_USD_CLK_S
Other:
- board size 130 x 85 mm -> 130 x 89 mm

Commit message: Placement fixes for routing; DRC rules scoped so net classes don't break fine-pitch pads
- hubrails: C611/C612 swap, C603-C608 rotated (pad 1 to hub pin), C609/C610
  east, pin 99 via room, VBUS-detect parts repacked
- right: C835/C836 rotated, RP2350 USB via room
- usbc: U501 south, U504/U503 straps rearranged for downstream escape vias
- zz_integration: R908 at the U901 CLK escape, TP1206/TP1202 moved
- power: C220/C114/R122 to bottom (sense pair + VIN via room)
- net class clearances 0.15; HV 0.3 mm spacing only for drawn copper
- DRC: 0 errors (unrouted only); docs/routing-notes/placement-fixes.md

Co-Authored-By: Claude Opus 5.5 <noreply@anthropic.com>
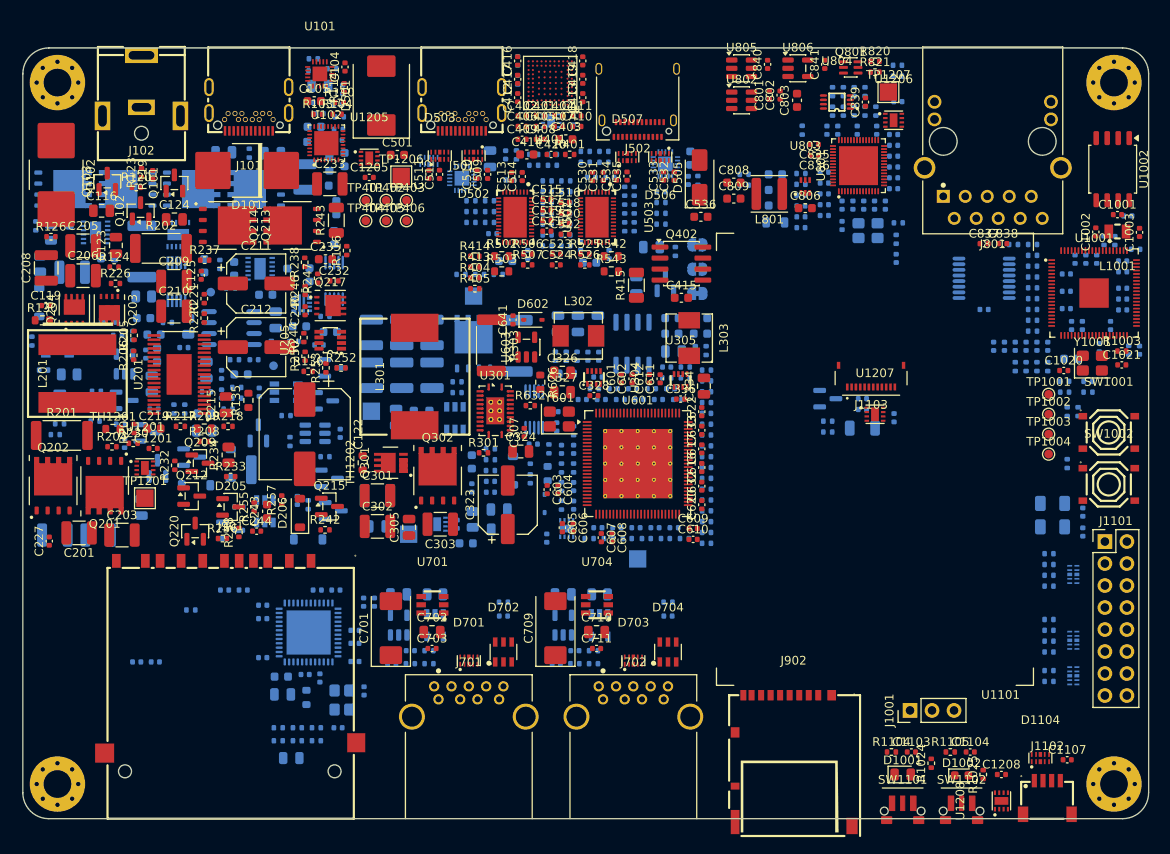
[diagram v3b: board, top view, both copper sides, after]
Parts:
- C114, C220, R122: moved to B.Cu
- moved R908 12.4 mm to (119.4, 114.9)
- moved TP1206 7.51 mm to (143.7, 64.8)
- moved C114 5.95 mm to (110.0, 81.5), turned to 0 degrees
- moved R410 5.90 mm to (173.7, 66.6)
- moved C220 5.25 mm to (115.5, 85.5)
- moved TP1202 4.25 mm to (108.1, 84.5)
- moved R122 4.15 mm to (110.3, 80.0), turned to 180 degrees
- moved R522 3.78 mm to (173.7, 70.3)
- moved R411 3.69 mm to (173.7, 67.8)
- moved C224 3.21 mm to (118.6, 84.6), turned to 0 degrees
- moved U504 3.20 mm to (174.2, 63.4)
- moved C537 3.15 mm to (177.1, 62.7), turned to -90 degrees
- moved C538 2.64 mm to (176.8, 65.3)
- moved R541 2.57 mm to (177.9, 65.3)
- moved R524 2.50 mm to (170.6, 70.6), turned to 90 degrees
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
